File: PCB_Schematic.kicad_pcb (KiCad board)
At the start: 2 copper layers, 78.9 x 94.7 mm, 107 parts, among them J1 Programming Header, J2 SDOAG_Connector, J3 Power_Connector, J4 Ultrasonic, J5 USB_A, J6 IMU_1, J7 IMU_2, Q1 BSS138, SW1 Reset Switch, U1 STM32F091RCTx, U2 FT232RL, U3 LM1117MP-ADJ, U4 TPS54331QDRQ1, U5 MAX7375AXR805

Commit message: buck
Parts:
- moved Cout1 20.1 mm to (113.8, 50.5), turned to 90 degrees
- moved Rfbb1 13.4 mm to (95.8, 53.1)
- moved Rfbt1 12.8 mm to (95.8, 57.1), turned to 0 degrees
- moved Cboot1 6.80 mm to (107.7, 50.8), turned to 90 degrees
- moved Ccomp2 6.14 mm to (100.3, 60.7), turned to 0 degrees
- moved D10 5.89 mm to (110.5, 50.5), turned to 90 degrees
- moved Ccomp1 5.55 mm to (100.3, 55.9), turned to 0 degrees
- moved L1 5.49 mm to (108.2, 57.7)
- moved Cin1 4.44 mm to (103.9, 44.7), turned to 0 degrees
- moved D11 3.89 mm to (96.0, 67.1), turned to 180 degrees
- moved R12 2.90 mm to (96.0, 70.4), turned to 180 degrees
- moved Rcomp1 2.34 mm to (100.3, 58.2), turned to 0 degrees
- moved Css1 0.57 mm to (99.1, 44.7)
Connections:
- net Net-(D10-K) renamed /Power Circuitry (Buck LDO Decoupling Caps)/PH
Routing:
- net Net-(U4-VSENSE): track 32.5 -> 7.65 mm
- net /Power Circuitry (Buck LDO Decoupling Caps)/PH: track 24.3 -> 0.00 mm
- net +3.3V: track 309.0 -> 298.9 mm, vias 7 -> 6
- net GND: track 66.4 -> 76.4 mm, vias 92 -> 112
- net +5V: track 266.5 -> 258.6 mm
- net Net-(U4-COMP): track 8.94 -> 6.33 mm
- net Net-(U4-BOOT): track 3.18 -> 5.12 mm, vias 0 -> 2
- net Net-(Ccomp2-Pad1): track 2.73 -> 3.38 mm
- added copper zone on F.Cu, net +5V
- added copper zone on F.Cu, net /Power Circuitry (Buck LDO Decoupling Caps)/PH
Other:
- board text added: "+"

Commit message: changes
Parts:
- removed the D14 at (99.1, 101.1)
- removed the D15 at (101.4, 116.4)
- removed the D17 at (154.9, 53.2)
- removed the D18 at (154.5, 108.6)
- removed the D19 at (147.3, 53.3)
- removed the R18 at (103.1, 101.1)
- removed the R19 at (106.5, 116.4)
- removed the R20 at (151.4, 58.4)
- removed the R21 at (154.2, 104.8)
- removed the R22 at (144.8, 51.8)
- removed the R24 at (155.7, 118.0)
- removed the R25 at (155.6, 88.8)
- removed the R26 at (154.5, 100.8)
- added D22: LED, LED_SMD:LED_0805_2012Metric_Pad1.15x1.40mm_HandSolder, F.Cu at (104.1, 116.1)
- added D25: LED, LED_SMD:LED_0805_2012Metric_Pad1.15x1.40mm_HandSolder, F.Cu at (155.7, 92.5)
- added D26: LED, LED_SMD:LED_0805_2012Metric_Pad1.15x1.40mm_HandSolder, F.Cu at (155.4, 97.3)
- added R27: 150, Resistor_SMD:R_0805_2012Metric_Pad1.20x1.40mm_HandSolder, F.Cu at (103.9, 101.6)
- added R28: 150, Resistor_SMD:R_0805_2012Metric_Pad1.20x1.40mm_HandSolder, F.Cu at (109.2, 116.1)
- added R29: 150, Resistor_SMD:R_0805_2012Metric_Pad1.20x1.40mm_HandSolder, F.Cu at (155.2, 104.9)
- added R30: 150, Resistor_SMD:R_0805_2012Metric_Pad1.20x1.40mm_HandSolder, F.Cu at (155.2, 117.3)
- added R31: 150, Resistor_SMD:R_0805_2012Metric_Pad1.20x1.40mm_HandSolder, F.Cu at (155.0, 88.9)
- added R32: 150, Resistor_SMD:R_0805_2012Metric_Pad1.20x1.40mm_HandSolder, F.Cu at (154.2, 101.1)
- C2, C3: moved to B.Cu
- D21, D23: value LED_Blue -> LED
- D24: value LED_Red -> LED
- U3: footprint Package_TO_SOT_SMD:SOT-223 -> Library:REALWORKLDOFT
- moved D21 56.9 mm to (99.3, 101.6), turned to 180 degrees
- moved D2 32.7 mm to (109.5, 65.5), turned to 0 degrees
- moved R2 28.4 mm to (109.7, 62.7), turned to 180 degrees
- moved D24 16.1 mm to (156.2, 113.3)
- moved D23 16.1 mm to (156.2, 108.4)
- moved R11 10.7 mm to (124.2, 39.4), turned to 90 degrees
- moved C2 9.55 mm to (122.9, 76.7), turned to 180 degrees
- moved R10 8.12 mm to (127.5, 39.6), turned to 90 degrees
- moved D9 6.26 mm to (120.4, 50.3)
- moved U3 6.13 mm to (120.9, 44.7), turned to 0 degrees
- moved C4 5.98 mm to (114.3, 45.7), turned to -90 degrees
- moved C13 5.68 mm to (128.0, 46.2), turned to 0 degrees
- moved C11 5.34 mm to (128.0, 43.4), turned to 0 degrees
- moved C3 4.97 mm to (127.3, 75.2), turned to 90 degrees
- moved FB1 1.92 mm to (132.6, 68.7), turned to 90 degrees
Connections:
- D21 pad 2: /SCL1E -> /TrigE
- D23 pad 2: /SDA2E -> /SDA1E
- D24 pad 2: /SCL2E -> /SCL1E
- U3 pad 4: (no net) -> +3.3V
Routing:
- net +3.3V: track 298.9 -> 272.2 mm, vias 6 -> 4
- net GND: track 76.4 -> 62.6 mm, vias 112 -> 93
- net Net-(C2-Pad1): track 6.83 -> 12.9 mm, vias 0 -> 1
- net Net-(D17-K): track 5.27 -> 0.00 mm
- net /Echo5VE: track 25.8 -> 21.3 mm
- net Net-(U3-ADJ/GND): track 6.59 -> 11.1 mm
- net Net-(D9-A): track 8.57 -> 12.8 mm, vias 0 -> 2
- net Net-(D14-K): track 4.08 -> 0.00 mm
- net Net-(D19-K): track 3.65 -> 0.00 mm
- net /SDA2: track 29.5 -> 26.2 mm, vias 2 -> 1
- net Net-(D26-K): track 0.00 -> 3.21 mm
- net Net-(D18-K): track 3.08 -> 0.00 mm
- net /USBD-: track 53.4 -> 50.3 mm
- net Net-(D22-K): track 0.00 -> 3.06 mm
- net Net-(D15-K): track 3.06 -> 0.00 mm
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- added copper zone on F.Cu, net +3.3V

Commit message: remove acute
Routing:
- net +5V: track 256.7 -> 259.2 mm
- net +3.3V: track 272.2 -> 273.5 mm
- net GND: track 62.6 -> 62.3 mm, vias 93 -> 97

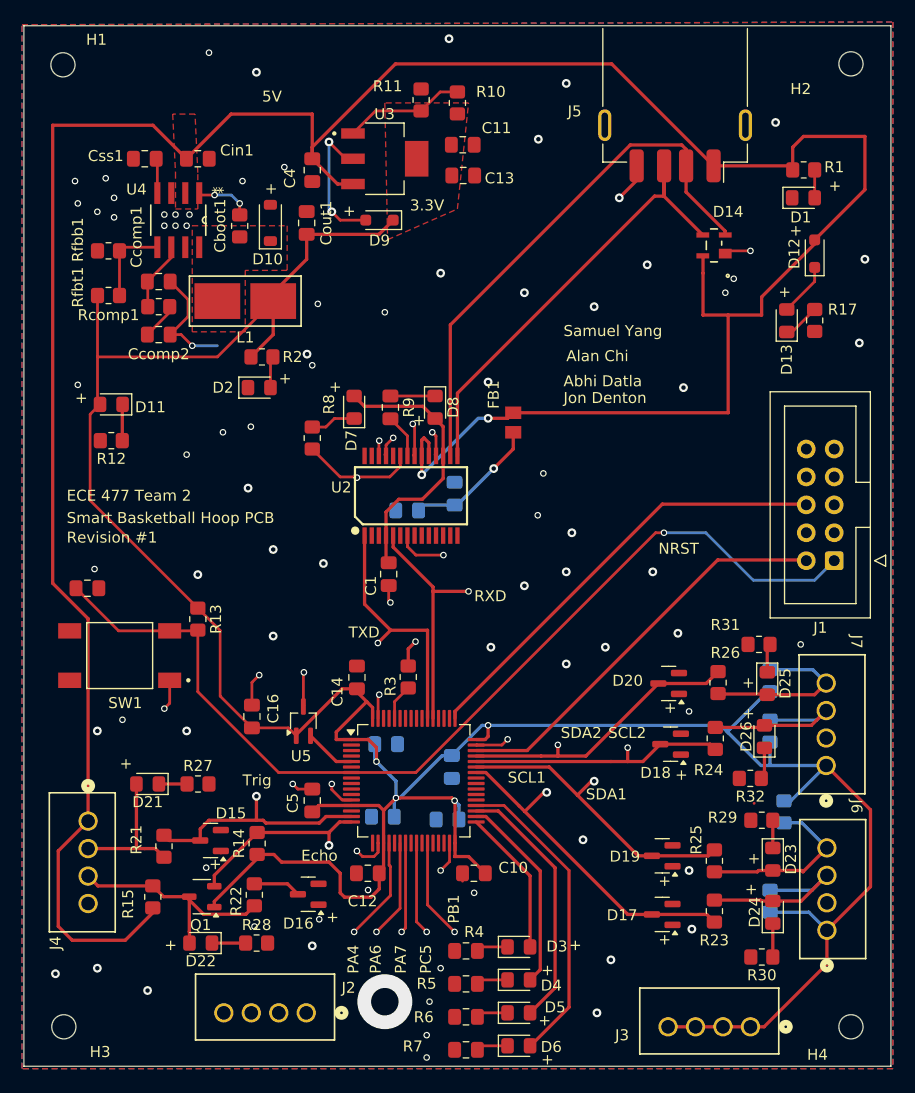
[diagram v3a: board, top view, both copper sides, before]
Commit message: added output plane for buck
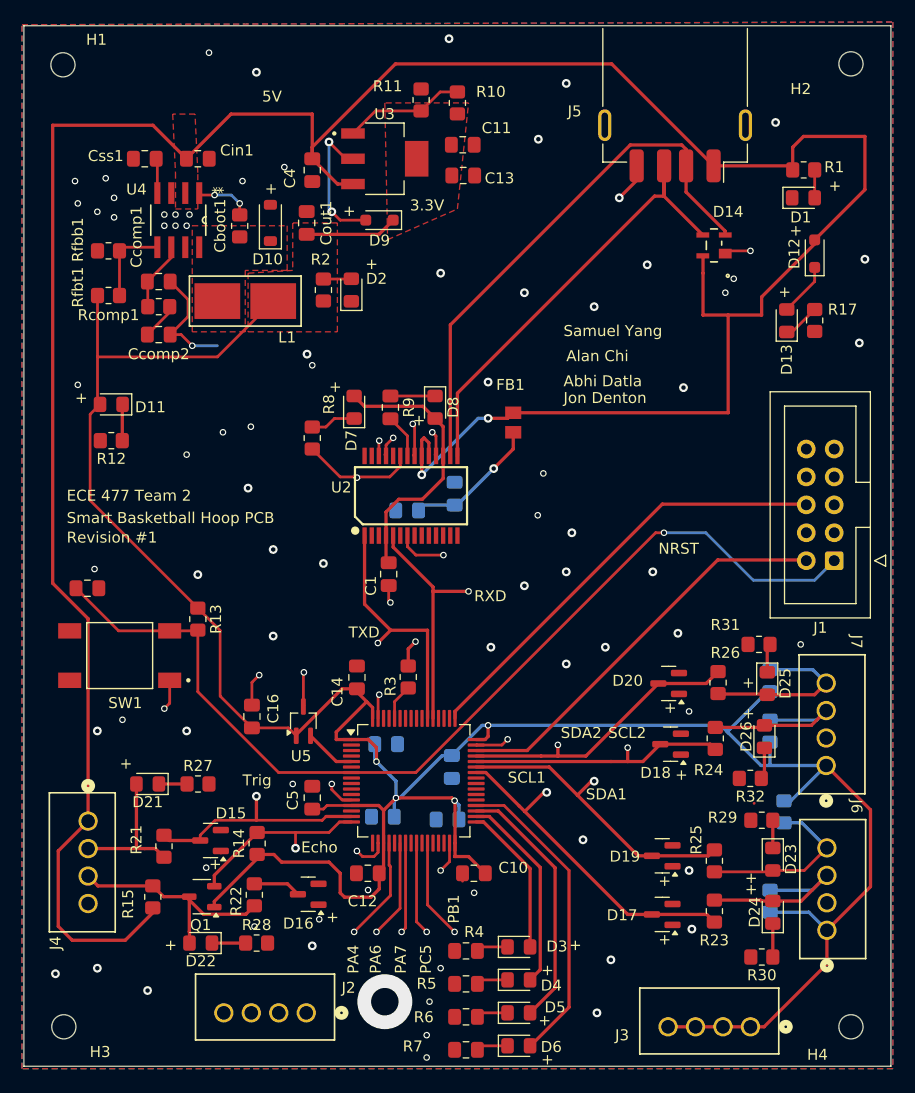
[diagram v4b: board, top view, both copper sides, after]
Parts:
- moved D2 12.2 mm to (117.9, 56.7), turned to 90 degrees
- moved R2 8.27 mm to (115.3, 56.6), turned to -90 degrees
- moved C5 0.25 mm to (114.3, 102.8)
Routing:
- net +3.3V: track 273.5 -> 260.9 mm
- net GND: track 62.3 -> 60.3 mm, vias 97 -> 95
- net /Trig: track 21.2 -> 20.6 mm

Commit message: most done
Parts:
- moved R3 1.63 mm to (121.4, 91.7)
- moved J2 1.54 mm to (113.5, 124.0)
- moved C1 0.65 mm to (120.7, 82.3)
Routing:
- net GND: track 60.3 -> 52.7 mm, vias 95 -> 97
- net /TXD: track 22.6 -> 20.7 mm
- net /RXD: track 21.4 -> 19.5 mm
- net +3.3V: track 260.9 -> 260.8 mm, vias 4 -> 5
- net +5V: vias 2 -> 3
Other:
- board text added: "CSA/CSM"
- board text added: "IMU1"
- board text added: "IMU2"
- board text added: "SD0AG"

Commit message: final sending for review
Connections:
- U3 pad 4: +3.3V -> Net-(D9-A)
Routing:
- net Net-(D9-A): track 12.8 -> 19.4 mm
- net +5V: track 259.2 -> 257.9 mm
- net +3.3V: track 260.8 -> 259.8 mm

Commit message: some changes
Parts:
- C1: moved to B.Cu
- C10: value 10 nF -> .1uF
- C12, C9: value 4.7 uF -> .1uF
- C14: value 1 uF -> .1uF
- C3: moved to F.Cu
- C5: value .1 uF -> 10nF
- C6, C8: value .1 uF -> 4.7uF
- C7: value .1 uF -> 1uF
- moved C1 7.09 mm to (120.4, 75.2), turned to 180 degrees
- moved C3 5.34 mm to (132.6, 75.0), turned to -90 degrees
- moved C2 2.79 mm to (125.7, 76.7)
- moved D13 2.54 mm to (160.0, 59.4)
- moved R17 2.54 mm to (157.5, 59.4)
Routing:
- net +5V: track 257.9 -> 262.4 mm
- net GND: track 52.7 -> 48.8 mm, vias 97 -> 96
- net /USB UART Comm/VCCIO: track 25.4 -> 23.4 mm, vias 0 -> 2
- net /USBD-: track 50.3 -> 52.2 mm
- net Net-(C2-Pad1): track 12.9 -> 11.3 mm
- net Net-(D12-K): track 4.88 -> 3.83 mm

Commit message: finish touches
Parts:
- moved FB1 1.59 mm to (133.3, 70.1), turned to 0 degrees
- turned C10 to 0 degrees
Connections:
- C2 pad 1: Net-(C2-Pad1) -> +5V
- C3 pad 1: Net-(C2-Pad1) -> +5V
- D12 pad 1: Net-(D12-K) -> +5V
- D12 pad 2: +5V -> Net-(D12-A)
- D13 pad 2: Net-(D12-K) -> +5V
- FB1 pad 1: Net-(C2-Pad1) -> +5V
- FB1 pad 2: +5V -> Net-(U2-VCC)
- J5 pad 1: +5V -> Net-(D12-A)
- U2 pad 20: +5V -> Net-(U2-VCC)
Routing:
- net Net-(U2-VCC): track 0.00 -> 16.0 mm, vias 0 -> 2
- net Net-(D12-A): track 0.00 -> 12.7 mm
- net Net-(C2-Pad1): track 11.3 -> 0.00 mm, vias 1 -> 0
- net Net-(D12-K): track 3.83 -> 0.00 mm
- net +5V: track 262.4 -> 261.2 mm, vias 3 -> 4
- net +3.3V: track 259.8 -> 260.9 mm
- net /Echo5VE: track 21.3 -> 20.5 mm
- net GND: track 48.8 -> 48.0 mm
